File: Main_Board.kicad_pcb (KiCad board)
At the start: 2 copper layers, 90 x 90 mm, 64 parts, among them J1 DAC_12-bits, J2 Measurement_Header, J3 8-Bit DAC_CEM_Control, Q1 Q_PNP_BCE, Q2 Q_NPN_BCE, U1 AD667, U2 LF356, U3 AD558JN

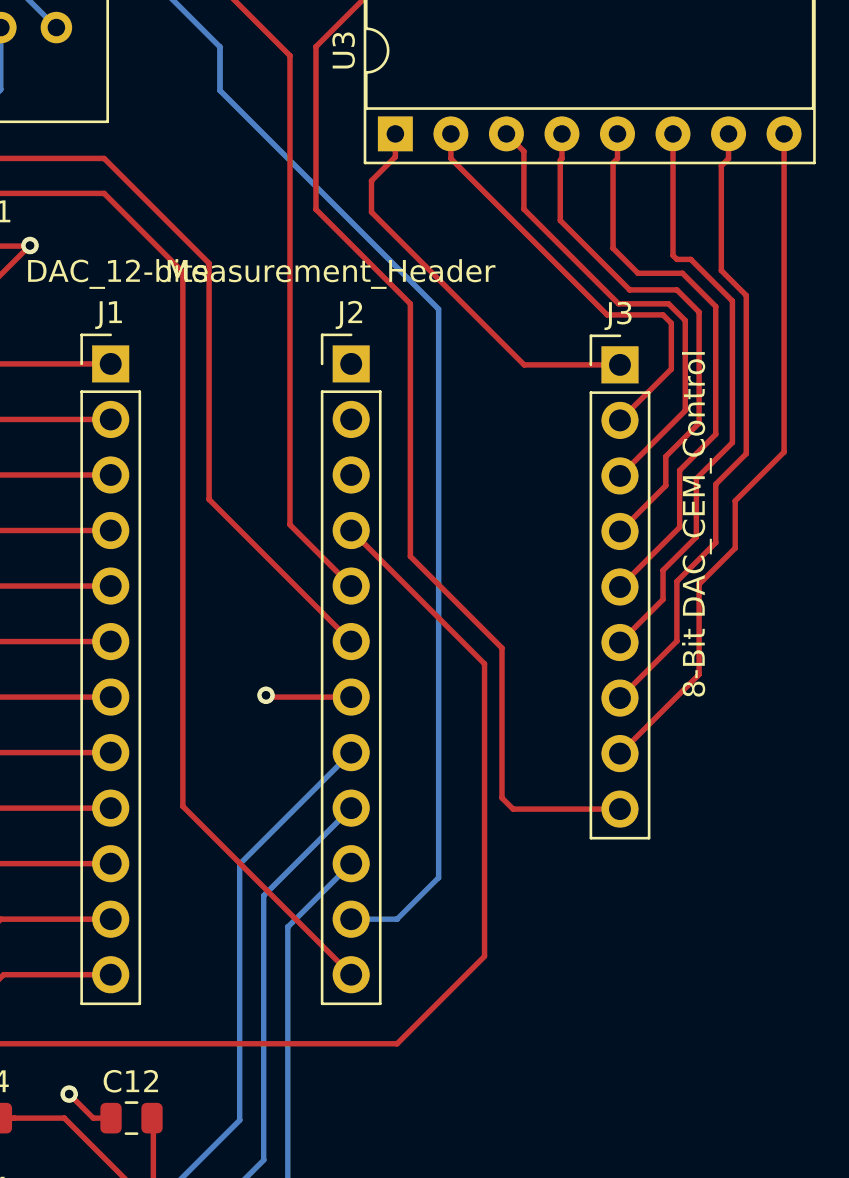
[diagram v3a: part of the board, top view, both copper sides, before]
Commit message: Added another 12-pin
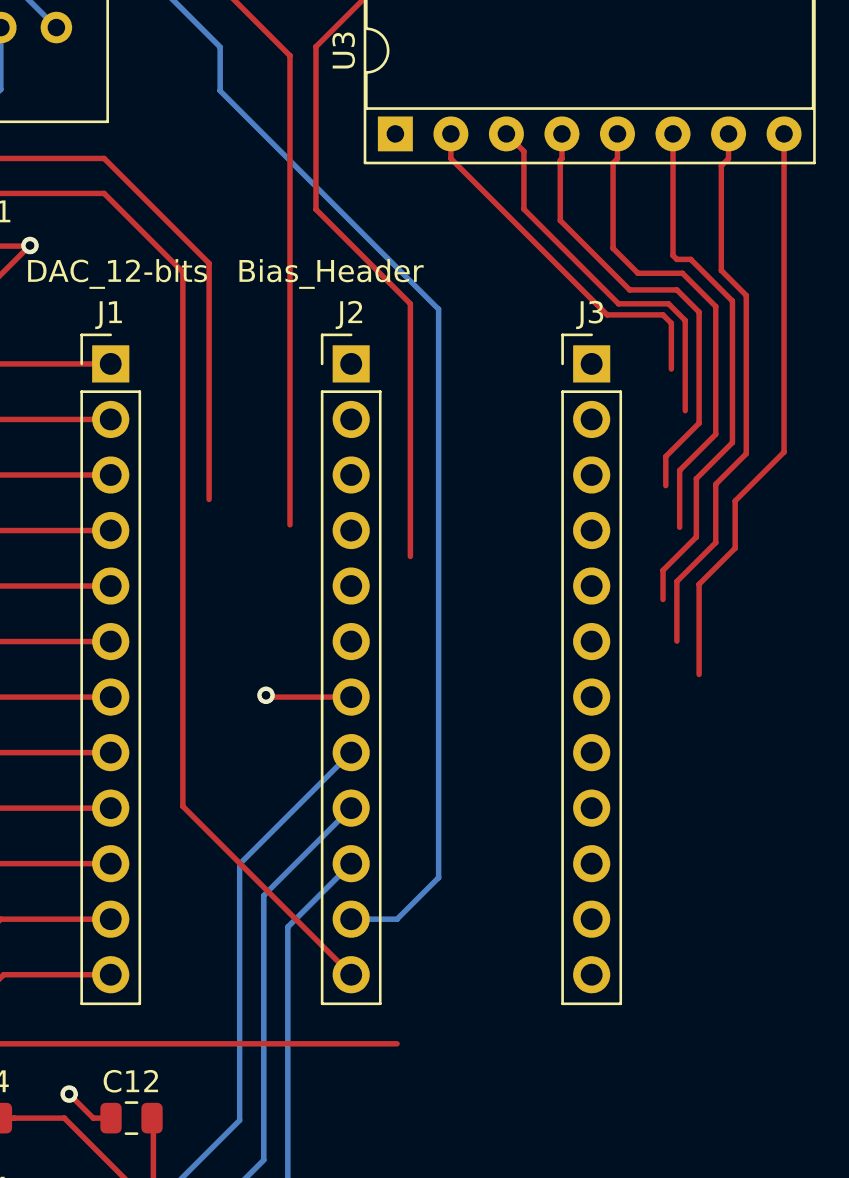
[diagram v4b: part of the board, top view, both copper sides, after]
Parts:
- J2: value Measurement_Header -> Bias_Header
- J3: value 8-Bit DAC_CEM_Control -> Measurement_Header; footprint Connector_PinHeader_2.54mm:PinHeader_1x09_P2.54mm_Vertical -> Connector_PinHeader_2.54mm:PinHeader_1x12_P2.54mm_Vertical
- moved J3 1.30 mm to (89.0, 115.5)
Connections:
- J2 pad 1: /MSP430_P2.5_filamentCurrent -> /-200V
- J2 pad 10: /-15V -> /+15V
- J2 pad 2: /MSP430_P2.6_transistorBaseVoltage -> Net-(J2-Pad2)
- J2 pad 3: /MSP430_P2.7_cemMeasure -> Net-(J2-Pad3)
- J2 pad 4: /+15V -> /-15V
- J2 pad 5: /+5V -> /-5V
- J2 pad 6: /+3V -> /-3V
- J2 pad 8: /-3V -> /+3V
- J2 pad 9: /-5V -> /+5V
- J3 pad 9: /CEM_Trans_Base_Vol -> Net-(J3-Pad9)
- U3 pad 15: /CEM_Trans_Base_Vol -> /MSP430_P2.6_transistorBaseVoltage
- U3 pad 16: /CEM_Trans_Base_Vol -> /MSP430_P2.6_transistorBaseVoltage
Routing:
- net /CEM_Trans_Base_Vol: track 51.2 -> 0.00 mm
- net /MSP430_P2.6_transistorBaseVoltage: track 0.00 -> 32.8 mm
- net /+15V: track 289.9 -> 262.2 mm
- net /MSP430_P2.4_Bit0: track 18.3 -> 0.00 mm
- net /+3V: track 85.9 -> 76.7 mm
- net /MSP430_P3.3_Bit7: track 31.5 -> 26.3 mm
- net /MSP430_P2.6_Bit2: track 21.6 -> 17.4 mm
- net /+5V: track 68.3 -> 64.4 mm
- net /MSP430_P3.0_Bit4: track 25.8 -> 21.9 mm
- net /MSP430_P3.2_Bit6: track 28.8 -> 25.1 mm
- net /MSP430_P2.5_Bit1: track 19.8 -> 16.4 mm
- net /MSP430_P2.7_Bit3: track 23.6 -> 20.6 mm
- net /MSP430_P3.1_Bit5: track 26.9 -> 24.1 mm

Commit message: Re-routing
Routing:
- net /MSP430_P2.6_transistorBaseVoltage: track 32.8 -> 55.4 mm
- net /MSP430_P2.4_Bit0: track 0.00 -> 14.9 mm
- net /MSP430_P3.3_Bit7: track 26.3 -> 31.9 mm
- net /MSP430_P3.2_Bit6: track 25.1 -> 28.4 mm
- net /MSP430_P2.6_Bit2: track 17.4 -> 20.5 mm
- net /MSP430_P3.0_Bit4: track 21.9 -> 25.0 mm
- net /MSP430_P3.1_Bit5: track 24.1 -> 26.3 mm
- net /MSP430_P2.7_Bit3: track 20.6 -> 22.7 mm
- net /MSP430_P2.5_Bit1: track 16.4 -> 18.4 mm
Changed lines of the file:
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@@
     (thickness 1.6)
     (drawings 11)
-    (tracks 506)
+    (tracks 498)
     (zones 0)
     (modules 64)
@@
   (layers
     (0 F.Cu signal)
-    (31 B.Cu signal hide)
+    (31 B.Cu signal)
     (32 B.Adhes user)
     (33 F.Adhes user)
@@
   (segment (start 81.15257 97.3576) (end 82.5612 97.3576) (width 0.25) (layer F.Cu) (net 47))
   (segment (start 80.0212 97.3576) (end 81.15257 97.3576) (width 0.25) (layer F.Cu) (net 47))
-  (segment (start 76.389 100.9898) (end 80.0212 97.3576) (width 0.25) (layer F.Cu) (net 47))
-  (segment (start 80.707 112.75) (end 76.389 108.432) (width 0.25) (layer F.Cu) (net 47))
-  (segment (start 76.389 108.432) (end 76.389 100.9898) (width 0.25) (layer F.Cu) (net 47))
-  (segment (start 80.707 124.307) (end 80.707 112.75) (width 0.25) (layer F.Cu) (net 47))
-  (segment (start 97.8012 104.9776) (end 97.8012 119.5318) (width 0.25) (layer F.Cu) (net 57))
-  (segment (start 97.8012 119.5318) (end 95.566 121.767) (width 0.25) (layer F.Cu) (net 57))
-  (segment (start 95.566 121.767) (end 95.566 123.926) (width 0.25) (layer F.Cu) (net 57))
-  (segment (start 95.566 123.926) (end 93.915 125.577) (width 0.25) (layer F.Cu) (net 57))
-  (segment (start 93.915 125.577) (end 93.915 129.7045) (width 0.25) (layer F.Cu) (net 57))
-  (segment (start 95.2612 106.10897) (end 94.931 106.43917) (width 0.25) (layer F.Cu) (net 58))
-  (segment (start 95.2612 104.9776) (end 95.2612 106.10897) (width 0.25) (layer F.Cu) (net 58))
-  (segment (start 94.931 106.43917) (end 94.931 111.226) (width 0.25) (layer F.Cu) (net 58))
-  (segment (start 94.931 111.226) (end 96.074 112.369) (width 0.25) (layer F.Cu) (net 58))
-  (segment (start 96.074 112.369) (end 96.074 119.608) (width 0.25) (layer F.Cu) (net 58))
-  (segment (start 96.074 119.608) (end 94.677 121.005) (width 0.25) (layer F.Cu) (net 58))
-  (segment (start 94.677 121.005) (end 94.677 123.672) (width 0.25) (layer F.Cu) (net 58))
-  (segment (start 94.677 123.672) (end 92.899 125.45) (width 0.25) (layer F.Cu) (net 58))
-  (segment (start 92.899 125.45) (end 92.899 128.1805) (width 0.25) (layer F.Cu) (net 58))
-  (segment (start 92.7212 104.9776) (end 92.7212 110.5402) (width 0.25) (layer F.Cu) (net 59))
-  (segment (start 92.7212 110.5402) (end 92.899 110.718) (width 0.25) (layer F.Cu) (net 59))
-  (segment (start 92.899 110.718) (end 93.534 110.718) (width 0.25) (layer F.Cu) (net 59))
-  (segment (start 93.534 110.718) (end 95.439 112.623) (width 0.25) (layer F.Cu) (net 59))
-  (segment (start 95.439 112.623) (end 95.439 119.1) (width 0.25) (layer F.Cu) (net 59))
-  (segment (start 95.439 119.1) (end 93.788 120.751) (width 0.25) (layer F.Cu) (net 59))
-  (segment (start 93.788 120.751) (end 93.788 123.418) (width 0.25) (layer F.Cu) (net 59))
-  (segment (start 93.788 123.418) (end 92.264 124.942) (width 0.25) (layer F.Cu) (net 59))
-  (segment (start 92.264 124.942) (end 92.264 126.2755) (width 0.25) (layer F.Cu) (net 59))
-  (segment (start 93.026 120.37) (end 93.026 122.9735) (width 0.25) (layer F.Cu) (net 60))
-  (segment (start 93.153 111.353) (end 94.677 112.877) (width 0.25) (layer F.Cu) (net 60))
+  (segment (start 80.707 135.147) (end 89 143.44) (width 0.25) (layer F.Cu) (net 47))
+  (segment (start 80.707 112.75) (end 80.707 135.147) (width 0.25) (layer F.Cu) (net 47))
+  (segment (start 76.389 108.432) (end 80.707 112.75) (width 0.25) (layer F.Cu) (net 47))
+  (segment (start 80.0212 97.3576) (end 76.389 100.9898) (width 0.25) (layer F.Cu) (net 47))
+  (segment (start 76.389 100.9898) (end 76.389 108.432) (width 0.25) (layer F.Cu) (net 47))
+  (segment (start 89.849999 132.430001) (end 89 133.28) (width 0.25) (layer F.Cu) (net 57))
+  (segment (start 96.8 125.48) (end 89.849999 132.430001) (width 0.25) (layer F.Cu) (net 57))
+  (segment (start 96.8 107.11017) (end 96.8 125.48) (width 0.25) (layer F.Cu) (net 57))
+  (segment (start 97.8012 104.9776) (end 97.8012 106.10897) (width 0.25) (layer F.Cu) (net 57))
+  (segment (start 97.8012 106.10897) (end 96.8 107.11017) (width 0.25) (layer F.Cu) (net 57))
+  (segment (start 95.2612 124.4788) (end 89 130.74) (width 0.25) (layer F.Cu) (net 58))
+  (segment (start 95.2612 104.9776) (end 95.2612 124.4788) (width 0.25) (layer F.Cu) (net 58))
+  (segment (start 94.6 122.6) (end 89 128.2) (width 0.25) (layer F.Cu) (net 59))
+  (segment (start 94.6 112.6) (end 94.6 122.6) (width 0.25) (layer F.Cu) (net 59))
+  (segment (start 92.7212 104.9776) (end 92.7212 110.7212) (width 0.25) (layer F.Cu) (net 59))
+  (segment (start 92.7212 110.7212) (end 94.6 112.6) (width 0.25) (layer F.Cu) (net 59))
   (segment (start 90.1812 104.9776) (end 90.1812 106.10897) (width 0.25) (layer F.Cu) (net 60))
-  (segment (start 94.677 112.877) (end 94.677 118.719) (width 0.25) (layer F.Cu) (net 60))
   (segment (start 90.1812 106.10897) (end 89.978 106.31217) (width 0.25) (layer F.Cu) (net 60))
-  (segment (start 91.121 111.353) (end 93.153 111.353) (width 0.25) (layer F.Cu) (net 60))
   (segment (start 89.978 106.31217) (end 89.978 110.21) (width 0.25) (layer F.Cu) (net 60))
-  (segment (start 94.677 118.719) (end 93.026 120.37) (width 0.25) (layer F.Cu) (net 60))
   (segment (start 89.978 110.21) (end 91.121 111.353) (width 0.25) (layer F.Cu) (net 60))
+  (segment (start 91.121 111.353) (end 92.253 111.353) (width 0.25) (layer F.Cu) (net 60))
+  (segment (start 92.253 111.353) (end 93.8 112.9) (width 0.25) (layer F.Cu) (net 60))
+  (segment (start 93.8 120.86) (end 89 125.66) (width 0.25) (layer F.Cu) (net 60))
+  (segment (start 93.8 112.9) (end 93.8 120.86) (width 0.25) (layer F.Cu) (net 60))
   (segment (start 87.6412 106.10897) (end 87.565 106.18517) (width 0.25) (layer F.Cu) (net 61))
   (segment (start 87.6412 104.9776) (end 87.6412 106.10897) (width 0.25) (layer F.Cu) (net 61))
   (segment (start 87.565 106.18517) (end 87.565 108.94) (width 0.25) (layer F.Cu) (net 61))
   (segment (start 87.565 108.94) (end 90.74 112.115) (width 0.25) (layer F.Cu) (net 61))
-  (segment (start 90.74 112.115) (end 92.899 112.115) (width 0.25) (layer F.Cu) (net 61))
-  (segment (start 92.899 112.115) (end 93.915 113.131) (width 0.25) (layer F.Cu) (net 61))
-  (segment (start 93.915 113.131) (end 93.915 118.211) (width 0.25) (layer F.Cu) (net 61))
-  (segment (start 93.915 118.211) (end 92.391 119.735) (width 0.25) (layer F.Cu) (net 61))
-  (segment (start 92.391 119.735) (end 92.391 121.0685) (width 0.25) (layer F.Cu) (net 61))
+  (segment (start 90.74 112.115) (end 91.815 112.115) (width 0.25) (layer F.Cu) (net 61))
+  (segment (start 91.815 112.115) (end 93 113.3) (width 0.25) (layer F.Cu) (net 61))
+  (segment (start 93 119.12) (end 89 123.12) (width 0.25) (layer F.Cu) (net 61))
+  (segment (start 93 113.3) (end 93 119.12) (width 0.25) (layer F.Cu) (net 61))
   (segment (start 85.901199 105.777599) (end 85.901199 108.419199) (width 0.25) (layer F.Cu) (net 62))
   (segment (start 85.1012 104.9776) (end 85.901199 105.777599) (width 0.25) (layer F.Cu) (net 62))
   (segment (start 85.901199 108.419199) (end 90.232 112.75) (width 0.25) (layer F.Cu) (net 62))
-  (segment (start 90.232 112.75) (end 92.518 112.75) (width 0.25) (layer F.Cu) (net 62))
-  (segment (start 92.518 112.75) (end 93.28 113.512) (width 0.25) (layer F.Cu) (net 62))
-  (segment (start 93.28 113.512) (end 93.28 117.6395) (width 0.25) (layer F.Cu) (net 62))
+  (segment (start 90.232 112.75) (end 91.35 112.75) (width 0.25) (layer F.Cu) (net 62))
+  (segment (start 91.35 112.75) (end 92.2 113.6) (width 0.25) (layer F.Cu) (net 62))
+  (segment (start 92.2 117.38) (end 89 120.58) (width 0.25) (layer F.Cu) (net 62))
+  (segment (start 92.2 113.6) (end 92.2 117.38) (width 0.25) (layer F.Cu) (net 62))
   (segment (start 82.5612 106.10897) (end 89.71023 113.258) (width 0.25) (layer F.Cu) (net 63))
   (segment (start 82.5612 104.9776) (end 82.5612 106.10897) (width 0.25) (layer F.Cu) (net 63))
-  (segment (start 89.71023 113.258) (end 92.264 113.258) (width 0.25) (layer F.Cu) (net 63))
-  (segment (start 92.264 113.258) (end 92.645 113.639) (width 0.25) (layer F.Cu) (net 63))
-  (segment (start 92.645 113.639) (end 92.645 115.7345) (width 0.25) (layer F.Cu) (net 63))
+  (segment (start 89.71023 113.258) (end 90.958 113.258) (width 0.25) (layer F.Cu) (net 63))
+  (segment (start 90.958 113.258) (end 91.4 113.7) (width 0.25) (layer F.Cu) (net 63))
+  (segment (start 91.4 115.64) (end 89 118.04) (width 0.25) (layer F.Cu) (net 63))
+  (segment (start 91.4 113.7) (end 91.4 115.64) (width 0.25) (layer F.Cu) (net 63))
+  (segment (start 87.9 115.5) (end 89 115.5) (width 0.25) (layer F.Cu) (net 64))
+  (segment (start 80.0212 107.6212) (end 87.9 115.5) (width 0.25) (layer F.Cu) (net 64))
+  (segment (start 80.0212 104.9776) (end 80.0212 107.6212) (width 0.25) (layer F.Cu) (net 64))
   (zone (net 1) (net_name GND) (layer B.Cu) (hatch edge 0.508)
     (connect_pads (clearance 0.508))
@@
     (connect_pads (clearance 0.508))
     (min_thickness 0.254)
-    (fill yes (arc_segments 32) (thermal_gap 0.508) (thermal_bridge_width 0.508))
+    (fill (arc_segments 32) (thermal_gap 0.508) (thermal_bridge_width 0.508))
     (polygon
       (pts

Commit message: Pins
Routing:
- net /Vin: track 148.1 -> 117.3 mm
- net /-15V: track 130.4 -> 107.1 mm
- net /-3V: track 70.3 -> 51.4 mm
- net /-5V: track 51.7 -> 33.9 mm
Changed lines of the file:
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@@
     (thickness 1.6)
     (drawings 11)
-    (tracks 498)
+    (tracks 489)
     (zones 0)
     (modules 64)
@@
   (segment (start 64.52 166.6) (end 68.9 166.6) (width 0.25) (layer B.Cu) (net 3))
   (segment (start 68.9 166.6) (end 75.1 160.4) (width 0.25) (layer B.Cu) (net 3))
-  (segment (start 75.1 141.26) (end 78 138.36) (width 0.25) (layer B.Cu) (net 3))
-  (segment (start 75.1 160.4) (end 75.1 141.26) (width 0.25) (layer B.Cu) (net 3))
   (segment (start 61.9508 154.8714) (end 67.0758 154.8714) (width 0.25) (layer F.Cu) (net 4))
   (segment (start 61.9508 158.9508) (end 64.46 161.46) (width 0.25) (layer F.Cu) (net 4))
@@
   (segment (start 67.0758 158.8442) (end 64.46 161.46) (width 0.25) (layer F.Cu) (net 4))
   (segment (start 67.0758 154.8714) (end 67.0758 158.8442) (width 0.25) (layer F.Cu) (net 4))
-  (segment (start 78 135.82) (end 74 139.82) (width 0.25) (layer B.Cu) (net 4))
   (segment (start 74 151.92) (end 64.46 161.46) (width 0.25) (layer B.Cu) (net 4))
-  (segment (start 74 139.82) (end 74 151.92) (width 0.25) (layer B.Cu) (net 4))
   (segment (start 44.6508 159.1508) (end 44.6508 154.6814) (width 0.25) (layer F.Cu) (net 5))
   (segment (start 46.96 161.46) (end 44.6508 159.1508) (width 0.25) (layer F.Cu) (net 5))
@@
   (segment (start 46.96 161.46) (end 61.54 161.46) (width 0.25) (layer B.Cu) (net 5))
   (segment (start 61.54 161.46) (end 72.9 150.1) (width 0.25) (layer B.Cu) (net 5))
-  (segment (start 72.9 138.38) (end 78 133.28) (width 0.25) (layer B.Cu) (net 5))
-  (segment (start 72.9 150.1) (end 72.9 138.38) (width 0.25) (layer B.Cu) (net 5))
   (segment (start 22.740997 108.625) (end 22.28233 109.083667) (width 0.25) (layer F.Cu) (net 6))
   (segment (start 28 108.625) (end 22.740997 108.625) (width 0.25) (layer F.Cu) (net 6))
@@
   (segment (start 54.365997 83.2) (end 51.28233 86.283667) (width 0.25) (layer F.Cu) (net 6))
   (segment (start 56.5 83.2) (end 54.365997 83.2) (width 0.25) (layer F.Cu) (net 6))
-  (segment (start 78 140.9) (end 80.1 140.9) (width 0.25) (layer B.Cu) (net 6))
-  (segment (start 80.1 140.9) (end 82 139) (width 0.25) (layer B.Cu) (net 6))
-  (segment (start 82 139) (end 82 113) (width 0.25) (layer B.Cu) (net 6))
   (segment (start 82 113) (end 72 103) (width 0.25) (layer B.Cu) (net 6))
   (segment (start 72 103) (end 72 101) (width 0.25) (layer B.Cu) (net 6))
